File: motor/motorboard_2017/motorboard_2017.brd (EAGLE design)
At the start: 50.8 x 50.8 mm, 42 parts, among them CON4 MOLEX_5566-2, CON5 S3B-PH-SM4-TB, CON6 S3B-PH-SM4-TB, U1 TEENSY_3.1_BASIC_2, U2 PCA9685PW, U4 TCAN1042HVDR

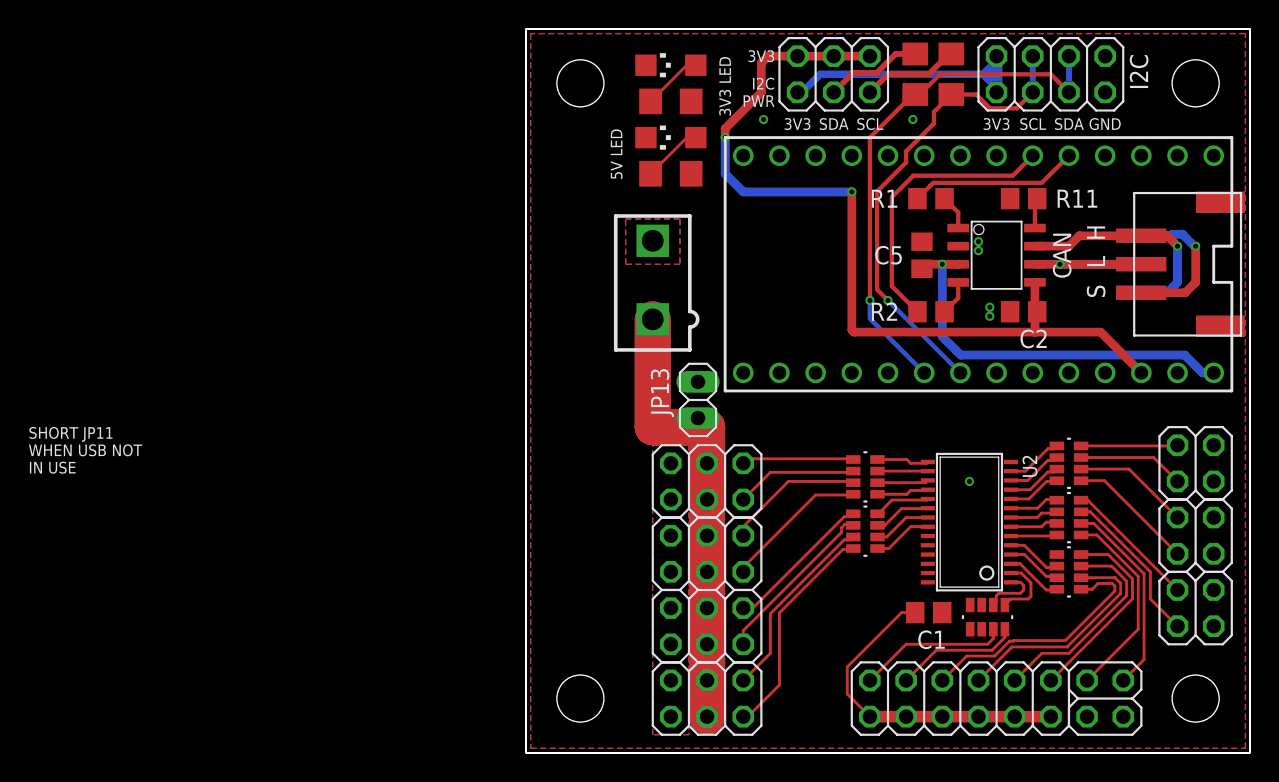
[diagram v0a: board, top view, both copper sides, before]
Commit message: Completed routing; Generated CAM files
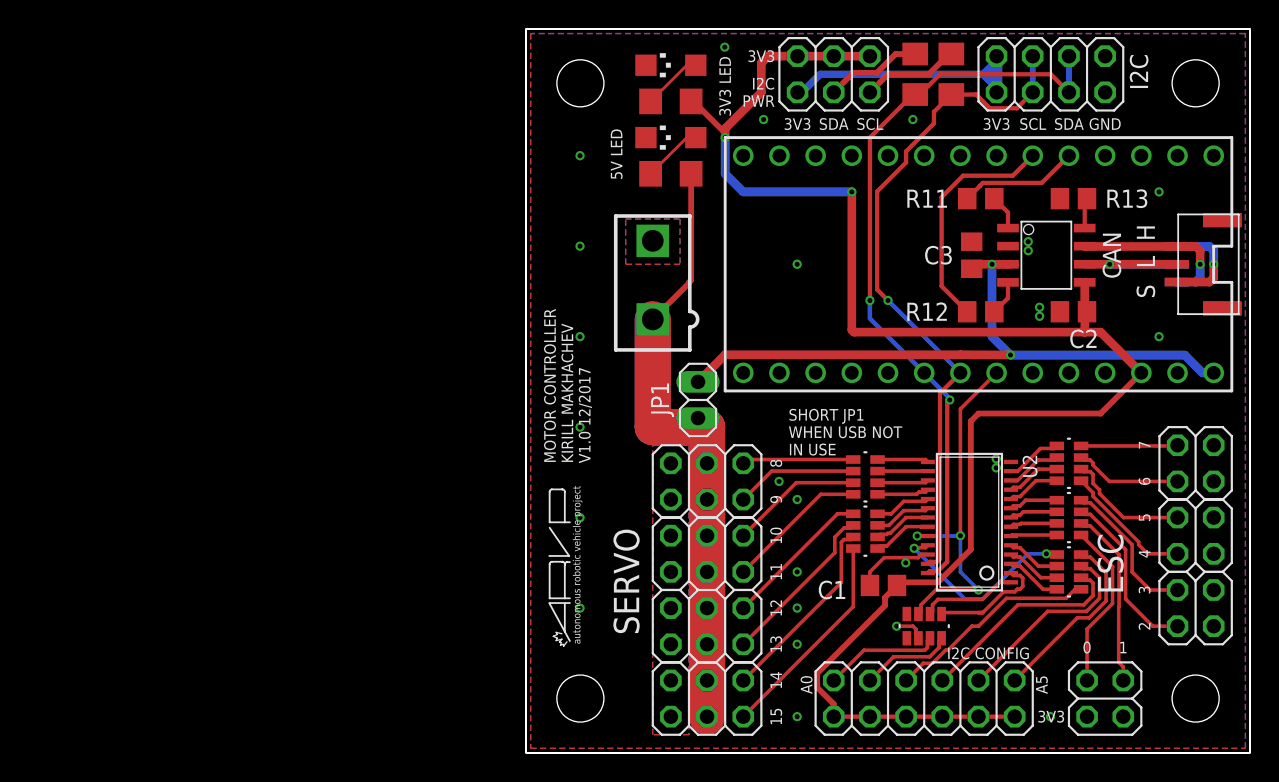
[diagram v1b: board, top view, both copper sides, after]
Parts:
- removed C5: 10u, rcl:C0805
- removed CON5, CON6: S3B-PH-SM4-TB, ARVP:S3B-PH-SM4-TB
- removed JP13: (no value), pinhead:1X02
- removed JP14: (no value), pinhead:2X04
- removed JP20: (no value), pinhead:2X06
- removed R23: 240, rcl:R1206
- removed R26: 580, rcl:R1206
- removed U4: TCAN1042HVDR, ARVP:SO-8
- added C3: 10u, rcl:C0805
- added CON2, CON3: SM03B-GHS-TB, ARVP:SM03B-GHS-TB
- added JP10, JP11, JP9: (no value), pinhead:2X02
- added R12: 220, rcl:R0805
- added R13: 1k, rcl:R0805
- added U$1: (no value), ARVP:LOGO2
- added U3: TCAN1042HVDR, ARVP:SO-8
- JP1: device pinhead:2X02 -> pinhead:1X02
- JP2: device pinhead:2X02 -> pinhead:2X06
- JP3: device pinhead:2X02 -> pinhead:2X03
- JP4: device pinhead:2X03 -> pinhead:2X04
- R1: value 220 -> 10k; device rcl:R0805 -> ARVP:EXBV8V-M
- R10, R9: value 10k -> 220
- R11: value 1k -> 220
- R2: value 220 -> 580; device rcl:R0805 -> rcl:R1206
- R3: value 10k -> 240
- R4: device rcl:R1206 -> ARVP:EXBV8V-M
- R5, R6: value 220 -> 10k; device ARVP:EXBV8V-M -> rcl:R1206
- moved JP1 37.9 mm to (120.0, 103.5), turned to 270 degrees
- moved JP3 37.3 mm to (129.5, 126.4)
- moved R4 35.9 mm to (146.1, 91.4), turned to 180 degrees
- moved R5 32.2 mm to (137.8, 126.4), turned to 270 degrees
- moved R1 30.0 mm to (135.9, 87.6), turned to 90 degrees
- moved R6 29.4 mm to (135.3, 126.4), turned to 270 degrees
- moved JP2 22.2 mm to (135.9, 82.5), turned to 0 degrees
- moved R2 20.7 mm to (118.1, 119.4)
- moved R3 17.3 mm to (118.1, 124.5), turned to 0 degrees
- moved JP4 15.2 mm to (144.8, 126.4)
- moved R8 15.1 mm to (146.1, 99.1), turned to 180 degrees
- moved R10 14.6 mm to (131.8, 94.3), turned to 0 degrees
- moved R7 14.6 mm to (146.1, 95.2), turned to 180 degrees
- moved R9 13.1 mm to (131.8, 98.1), turned to 0 degrees
- moved LED1 5.08 mm to (118.1, 121.9)
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- renumbered CON4 to CON1, JP15 to JP12, JP21 to JP5, JP22 to JP6, JP23 to JP7, JP24 to JP8
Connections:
- removed net A10: R9.5, U2.2
- removed net A11: R9.6, U2.1
- removed net A6: R10.5, U2.24
- removed net A7: R10.6, U2.5
- removed net A8: R10.7, U2.4
- removed net A9: R10.8, U2.3
- removed net PWM_CH16: R5.8, U2.6
- removed net PWM_CH17: R5.7, U2.7
- removed net PWM_CH18: R5.6, U2.8
- removed net PWM_CH19: R5.5, U2.9
- removed net PWM_CH20: R6.8, U2.10
- removed net PWM_CH21: R6.7, U2.11
- removed net PWM_CH22: R6.6, U2.12
- removed net PWM_CH23: R6.5, U2.13
- removed net PWM_CH24: R7.8, U2.15
- removed net PWM_CH25: R7.7, U2.16
- removed net PWM_CH26: R7.6, U2.17
- removed net PWM_CH27: R7.5, U2.18
- removed net PWM_CH28: R8.8, U2.19
- removed net PWM_CH29: R8.7, U2.20
- removed net PWM_CH30: R8.6, U2.21
- removed net PWM_CH31: R8.5, U2.22
- new net A0: R1.6, U2.1
- new net A1: R1.5, U2.2
- new net A2: R4.8, U2.3
- new net A3: R4.7, U2.4
- new net A4: R4.6, U2.5
- new net A5+1: JP2.12, R4.4
- new net PWM_CH0: R7.8, U2.6
- new net PWM_CH1: R7.7, U2.7
- new net PWM_CH10: R9.6, U2.17
- new net PWM_CH11: R9.5, U2.18
- new net PWM_CH12: R10.8, U2.19
- new net PWM_CH13: R10.7, U2.20
- new net PWM_CH14: R10.6, U2.21
- new net PWM_CH15: R10.5, U2.22
- new net PWM_CH2: R7.6, U2.8
- new net PWM_CH3: R7.5, U2.9
- new net PWM_CH4: R8.8, U2.10
- new net PWM_CH5: R8.7, U2.11
- new net PWM_CH6: R8.6, U2.12
- new net PWM_CH7: R8.5, U2.13
- new net PWM_CH8: R9.8, U2.15
- new net PWM_CH9: R9.7, U2.16
- net +3V3: now also JP2.1, JP2.11, JP2.3, JP2.5, JP2.7, JP2.9, JP3.1, JP3.3, JP3.5, R3.2, U3.5; no longer JP20.1, JP20.11, JP20.3, JP20.5, JP20.7, JP20.9, JP4.1, JP4.3, JP4.5, R23.2, U4.5
- net +5V: now also JP1.2, R2.2; no longer JP13.2, R26.2
- net A0+1: now also JP2.2, R1.3; no longer JP20.2, R9.3
- net A1+1: now also JP2.4, R1.4; no longer JP20.4, R9.4
- net A2+1: now also JP2.6, R4.1; no longer JP20.6, R10.1
- net A3+1: now also JP2.8, R4.2; no longer JP20.8, R10.2
- net A4+1: now also JP2.10, R4.3; no longer JP20.10, R10.3
- net A5: now also R4.5, U2.24; no longer JP20.12, R10.4
- net CANH1: now also CON2.P$3, CON3.P$3, U3.7; no longer CON5.P$3, CON6.P$3, U4.7
- net CANL1: now also CON2.P$2, CON3.P$2, U3.6; no longer CON5.P$2, CON6.P$2, U4.6
- net CANSH1: now also CON2.P$1, CON3.P$1; no longer CON5.P$1, CON6.P$1
- net CAN_RX1: now also R12.2, U3.4; no longer R2.2, U4.4
- net CAN_RX_T: now also R12.1; no longer R2.1
- net CAN_TX2: now also R11.2, U3.1; no longer R1.2, U4.1
- net CAN_TX_T: now also R11.1; no longer R1.1
- net GND: now also C3.2, CON2.P$4, CON2.P$5, CON3.P$4, CON3.P$5, JP10.1, JP10.2, JP11.1, JP11.2, JP4.1, JP4.2, JP9.1, JP9.2, R1.2, R13.1, U3.2; no longer C5.2, CON5.P$4, CON5.P$5, CON6.P$4, CON6.P$5, JP1.1, JP1.2, JP14.1, JP14.2, JP2.1, JP2.2, JP3.1, JP3.2, R11.1, R9.2, U4.2
- net I2C_3V1: now also JP3.6, JP4.7, JP4.8; no longer JP14.7, JP14.8, JP4.6
- net N$1: now also LED2.A, R3.1; no longer LED1.A, R23.1
- net N$2: now also LED1.A, R2.1; no longer LED2.A, R26.1
- net PCA_OE: now also R1.7, U1.20/A6; no longer R9.7
- net PWM_ESC0: now also R7.1; no longer R5.1
- net PWM_ESC1: now also R7.2; no longer R5.2
- net PWM_ESC2: now also JP9.4, R7.3; no longer JP1.4, R5.3
- net PWM_ESC3: now also JP9.3, R7.4; no longer JP1.3, R5.4
- net PWM_ESC4: now also JP11.4, R8.1; no longer JP2.4, R6.1
- net PWM_ESC5: now also JP11.3, R8.2; no longer JP2.3, R6.2
- net PWM_ESC6: now also JP10.4, R8.3; no longer JP3.4, R6.3
- net PWM_ESC7: now also JP10.3, R8.4; no longer JP3.3, R6.4
- net PWM_SERVO0: now also R9.1; no longer R7.1
- net PWM_SERVO1: now also R9.2; no longer R7.2
- net PWM_SERVO2: now also R9.3; no longer R7.3
- net PWM_SERVO3: now also R9.4; no longer R7.4
- net PWM_SERVO4: now also R10.1; no longer R8.1
- net PWM_SERVO5: now also R10.2; no longer R8.2
- net PWM_SERVO6: now also R10.3; no longer R8.3
- net PWM_SERVO7: now also R10.4; no longer R8.4
- net SCL: now also JP4.5, JP4.6, R5.2; no longer JP14.5, JP14.6, R4.2
- net SCL_3V1: now also JP3.2, R5.1; no longer JP4.2, R4.1
- net SDA: now also JP4.3, JP4.4, R6.2; no longer JP14.3, JP14.4, R3.2
- net SDA_3V1: now also JP3.4, R6.1; no longer JP4.4, R3.1
- net STB1: now also R13.2, U3.8; no longer R11.2, U4.8
- net VIN: now also C3.1, JP1.1, U3.3; no longer C5.1, JP13.1, U4.3
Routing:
- net +3V3: track 84.3 -> 119.9 mm
- net PCA_OE: track 0.00 -> 25.8 mm, vias 0 -> 3
- net VIN: track 28.1 -> 47.3 mm, vias 1 -> 2
- net SDA: track 37.0 -> 52.7 mm, vias 1 -> 2
- net SCL: track 33.2 -> 47.9 mm
- net A5+1: track 0.00 -> 13.0 mm
- net +5V: track 63.4 -> 74.7 mm
- net A1: track 0.00 -> 8.36 mm
- net GND: track 0.00 -> 7.68 mm, vias 7 -> 27
- net A0: track 0.00 -> 6.88 mm
- net A10: track 4.71 -> 0.00 mm
- net PWM_CH15: track 0.00 -> 4.17 mm
- net PWM_CH31: track 4.17 -> 0.00 mm
- net A11: track 4.12 -> 0.00 mm
- net PWM_CH30: track 4.10 -> 0.00 mm
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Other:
- board text added: "0"
- board text added: "1"
- board text added: "10"
- board text added: "11"
- board text added: "12"
- board text added: "13"
- board text added: "14"
- board text added: "15"
- board text added: "2"
- board text added: "3"
- board text added: "4"
- board text added: "5"
- board text added: "6"
- board text added: "7"
- board text added: "8"
- board text added: "9"
- board text added: "A0"
- board text added: "A5"
- board text added: "ESC"
- board text added: "I2C CONFIG"
- board text added: "MOTOR CONTROLLER KIRILL MAKHACHEV V1.0 12/2017"
- board text added: "SERVO"
- board text added: "SHORT JP1 WHEN USB NOT IN USE"
- board text removed: "Assumptions: this board is installed in right/rear or left/front section of robot. Teensy USB connector and CAN connector should point towards the center of hull. Mounting holes come from Sparkfun library, located in projects folder. Layout can be changed if needed, as long as USB and CAN guidelines are followed."
- board text removed: "Bottom"
- board text removed: "SHORT JP11 WHEN USB NOT IN USE"
- board text removed: "Towards acrylic wall"
- board text removed: "Towards middle of robot"
